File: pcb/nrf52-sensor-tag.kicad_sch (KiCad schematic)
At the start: 20 parts, among them IC1 LTR-308ALS-01, IC3 MS860702BA01-50, J3 Conn_01x07_Male, SW1 EVQ-PUA02K, SW2 EVQ-PUA02K, U1 MS88SF2

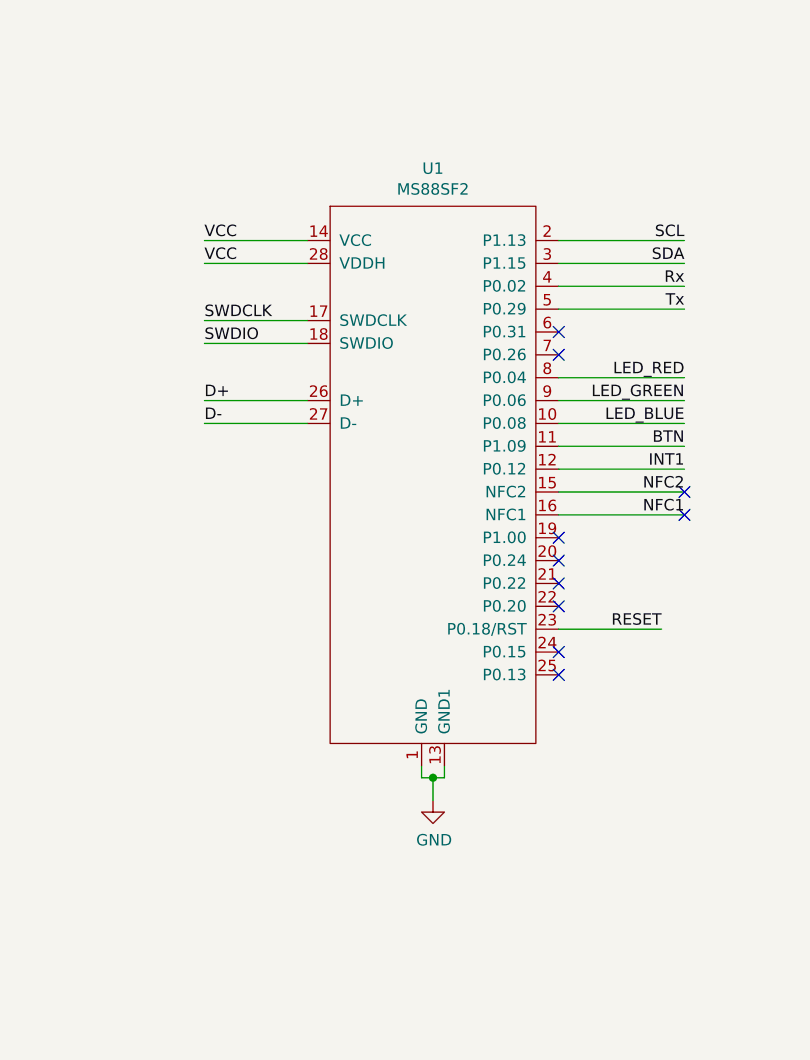
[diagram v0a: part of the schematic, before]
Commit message: Added PWR_FLAG to power tracks
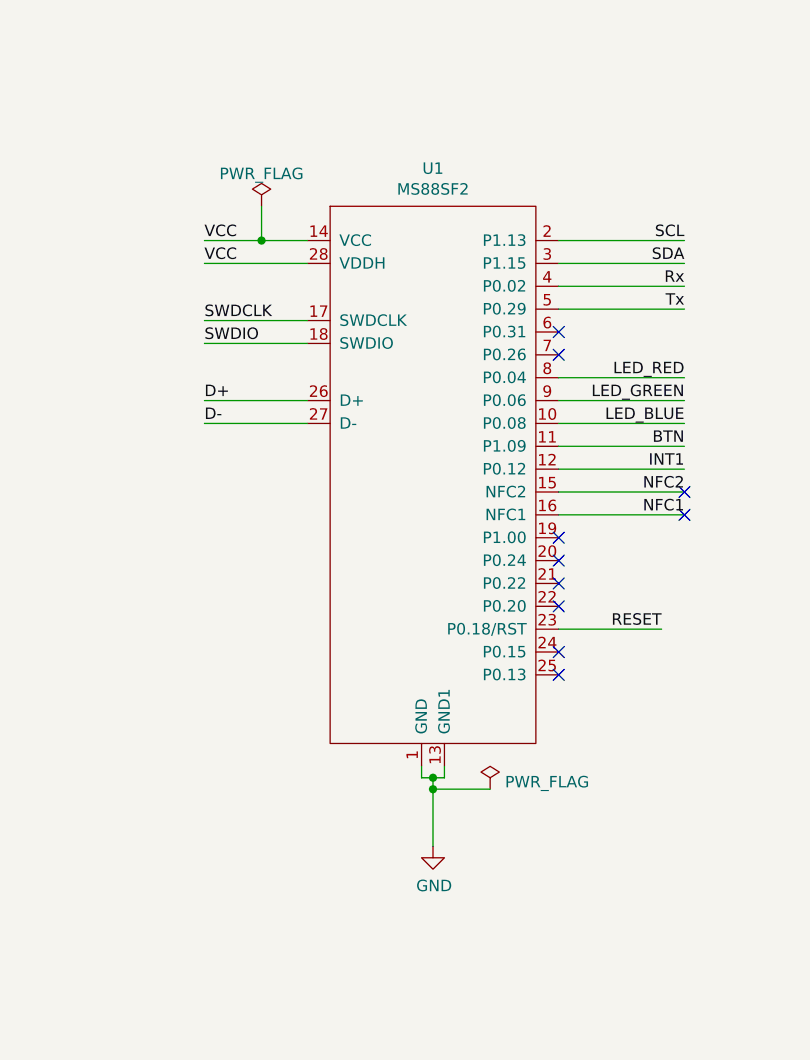
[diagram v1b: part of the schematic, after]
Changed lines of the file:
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@@
   (junction (at 62.23 104.14) (diameter 0) (color 0 0 0 0)
+  )
+  (junction (at 62.23 105.41) (diameter 0) (color 0 0 0 0)
+  )
+  (junction (at 43.18 44.45) (diameter 0) (color 0 0 0 0)
   )
   (junction (at 138.43 116.84) (diameter 0) (color 0 0 0 0)
@@
     (stroke (width 0) (type default) (color 0 0 0 0))
   )
+  (wire (pts (xy 60.96 104.14) (xy 62.23 104.14))
+    (stroke (width 0) (type default) (color 0 0 0 0))
+  )
+  (wire (pts (xy 48.26 55.88) (xy 36.83 55.88))
+    (stroke (width 0) (type default) (color 0 0 0 0))
+  )
+  (wire (pts (xy 52.07 173.99) (xy 50.8 173.99))
+    (stroke (width 0) (type default) (color 0 0 0 0))
+  )
+  (wire (pts (xy 214.63 48.26) (xy 214.63 45.72))
+    (stroke (width 0) (type default) (color 0 0 0 0))
+  )
+  (wire (pts (xy 68.58 105.41) (xy 62.23 105.41))
+    (stroke (width 0) (type default) (color 0 0 0 0))
+  )
+  (wire (pts (xy 90.17 52.07) (xy 76.2 52.07))
+    (stroke (width 0) (type default) (color 0 0 0 0))
+  )
+  (wire (pts (xy 43.18 40.64) (xy 43.18 44.45))
+    (stroke (width 0) (type default) (color 0 0 0 0))
+  )
   (wire (pts (xy 62.23 104.14) (xy 63.5 104.14))
     (stroke (width 0) (type default) (color 0 0 0 0))
   )
-  (wire (pts (xy 48.26 55.88) (xy 36.83 55.88))
-    (stroke (width 0) (type default) (color 0 0 0 0))
-  )
-  (wire (pts (xy 52.07 173.99) (xy 50.8 173.99))
-    (stroke (width 0) (type default) (color 0 0 0 0))
-  )
-  (wire (pts (xy 214.63 48.26) (xy 214.63 45.72))
-    (stroke (width 0) (type default) (color 0 0 0 0))
-  )
-  (wire (pts (xy 90.17 52.07) (xy 76.2 52.07))
-    (stroke (width 0) (type default) (color 0 0 0 0))
-  )
   (wire (pts (xy 167.64 139.7) (xy 161.29 139.7))
     (stroke (width 0) (type default) (color 0 0 0 0))
@@
     (stroke (width 0) (type default) (color 0 0 0 0))
   )
-  (wire (pts (xy 48.26 44.45) (xy 36.83 44.45))
+  (wire (pts (xy 48.26 44.45) (xy 43.18 44.45))
     (stroke (width 0) (type default) (color 0 0 0 0))
   )
@@
     (stroke (width 0) (type default) (color 0 0 0 0))
   )
+  (wire (pts (xy 62.23 104.14) (xy 62.23 105.41))
+    (stroke (width 0) (type default) (color 0 0 0 0))
+  )
   (polyline (pts (xy 186.69 87.63) (xy 284.48 87.63))
     (stroke (width 0) (type default) (color 0 0 0 0))
@@
     (stroke (width 0) (type default) (color 0 0 0 0))
   )
-  (wire (pts (xy 62.23 104.14) (xy 62.23 106.68))
+  (wire (pts (xy 62.23 105.41) (xy 62.23 111.76))
     (stroke (width 0) (type default) (color 0 0 0 0))
   )
@@
     (stroke (width 0) (type default) (color 0 0 0 0))
   )
-  (wire (pts (xy 60.96 104.14) (xy 62.23 104.14))
+  (wire (pts (xy 43.18 44.45) (xy 36.83 44.45))
     (stroke (width 0) (type default) (color 0 0 0 0))
   )
@@
     (pin "9")
   )
-  (symbol (lib_id "power:GND") (at 62.23 106.68 0) (unit 1)
-    (in_bom yes) (on_board yes)
-    (property "Reference" "#PWR0101" (id 0) (at 62.23 113.03 0)
-      (effects (font (size 1.27 1.27)) hide)
-    )
-    (property "Value" "GND" (id 1) (at 62.357 111.0742 0))
-    (property "Footprint" "" (id 2) (at 62.23 106.68 0)
-      (effects (font (size 1.27 1.27)) hide)
-    )
-    (property "Datasheet" "" (id 3) (at 62.23 106.68 0)
+  (symbol (lib_id "power:GND") (at 62.23 111.76 0) (unit 1)
+    (in_bom yes) (on_board yes)
+    (property "Reference" "#PWR0101" (id 0) (at 62.23 118.11 0)
+      (effects (font (size 1.27 1.27)) hide)
+    )
+    (property "Value" "GND" (id 1) (at 62.357 116.1542 0))
+    (property "Footprint" "" (id 2) (at 62.23 111.76 0)
+      (effects (font (size 1.27 1.27)) hide)
+    )
+    (property "Datasheet" "" (id 3) (at 62.23 111.76 0)
       (effects (font (size 1.27 1.27)) hide)
     )
@@
     (pin "1")
   )
+  (symbol (lib_id "power:PWR_FLAG") (at 43.18 40.64 0) (unit 1)
+    (in_bom yes) (on_board yes) (fields_autoplaced)
+    (property "Reference" "#FLG0102" (id 0) (at 43.18 38.735 0)
+      (effects (font (size 1.27 1.27)) hide)
+    )
+    (property "Value" "PWR_FLAG" (id 1) (at 43.18 37.0355 0))
+    (property "Footprint" "" (id 2) (at 43.18 40.64 0)
+      (effects (font (size 1.27 1.27)) hide)
+    )
+    (property "Datasheet" "~" (id 3) (at 43.18 40.64 0)
+      (effects (font (size 1.27 1.27)) hide)
+    )
+    (pin "1")
+  )
   (symbol (lib_id "power:GND") (at 220.98 130.81 0) (unit 1)
     (in_bom yes) (on_board yes)
@@
     (pin "1")
     (pin "2")
+  )
+  (symbol (lib_id "power:PWR_FLAG") (at 68.58 105.41 0) (unit 1)
+    (in_bom yes) (on_board yes) (fields_autoplaced)
+    (property "Reference" "#FLG0101" (id 0) (at 68.58 103.505 0)
+      (effects (font (size 1.27 1.27)) hide)
+    )
+    (property "Value" "PWR_FLAG" (id 1) (at 70.231 104.619 0)
+      (effects (font (size 1.27 1.27)) (justify left))
+    )
+    (property "Footprint" "" (id 2) (at 68.58 105.41 0)
+      (effects (font (size 1.27 1.27)) hide)
+    )
+    (property "Datasheet" "~" (id 3) (at 68.58 105.41 0)
+      (effects (font (size 1.27 1.27)) hide)
+    )
+    (pin "1")
   )
   (symbol (lib_id "LTR-308ALS-01:LTR-308ALS-01") (at 231.14 124.46 0) (unit 1)
@@
   )
   (symbol_instances
+    (path "/d83a379d-e68c-4c1d-b052-d16f1fa36678"
+      (reference "#FLG0101") (unit 1) (value "PWR_FLAG") (footprint "")
+    )
+    (path "/1679624a-0587-496f-b717-2bf6f3611773"
+      (reference "#FLG0102") (unit 1) (value "PWR_FLAG") (footprint "")
+    )
     (path "/00000000-0000-0000-0000-000060382555"
       (reference "#PWR0101") (unit 1) (value "GND") (footprint "")
